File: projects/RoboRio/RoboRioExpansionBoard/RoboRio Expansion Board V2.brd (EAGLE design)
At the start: 56.6 x 77.5 mm, 133 parts, among them J1 RRINTERFACE-FEMALE, J10 SPI_MISO, J11 SPI_MOSI, J12 I2C_SCL, J13 I2C_SDA, J14 UART_TX, J15 UART_RX, J16 LCD, J17 ADC1, J18 ADC2, J19 ADC3, J2 MICROSD-HINGED, J20 ADC4, J21 ADC5, J22 ADC6, J23 ADC7, J25 PWM0, J26 PWM1, J27 PWM2, J28 PWM3, J29 PWM4, J3 51387-0578, J30 PWM5, J31 PWM6, J32 PWM7, J33 PWM8, J34 PWM9, J35 AI0, J36 AI1, J37 AI2, J38 AI3, J39 AO0, J4 GPIO0, J40 AO1, J5 GPIO1, J6 GPIO2, J7 GPIO3, J8 SPI_CS, J9 SPI_CLK, Q1 NPN-SOT416, Q2 NPN-SOT416, Q3 NPN-SOT416, SW1 450-1781-ND, U1 FTS31XS-U, U2 24LC256ST, U3 REG1117, U4 TPS2115APWR, U5 P8X32A-Q44_P, U6 TC54VN43, U7 ADC124S01, U8 ADC124S01, Y1 5MHz

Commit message: More silk
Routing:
- net +3V3: track 245.5 -> 244.4 mm
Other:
- board text added: "8"
- board text added: "9"
- board text added: "R11 R12 R13 R14 R15 R16"
- board text added: "RR PWM"

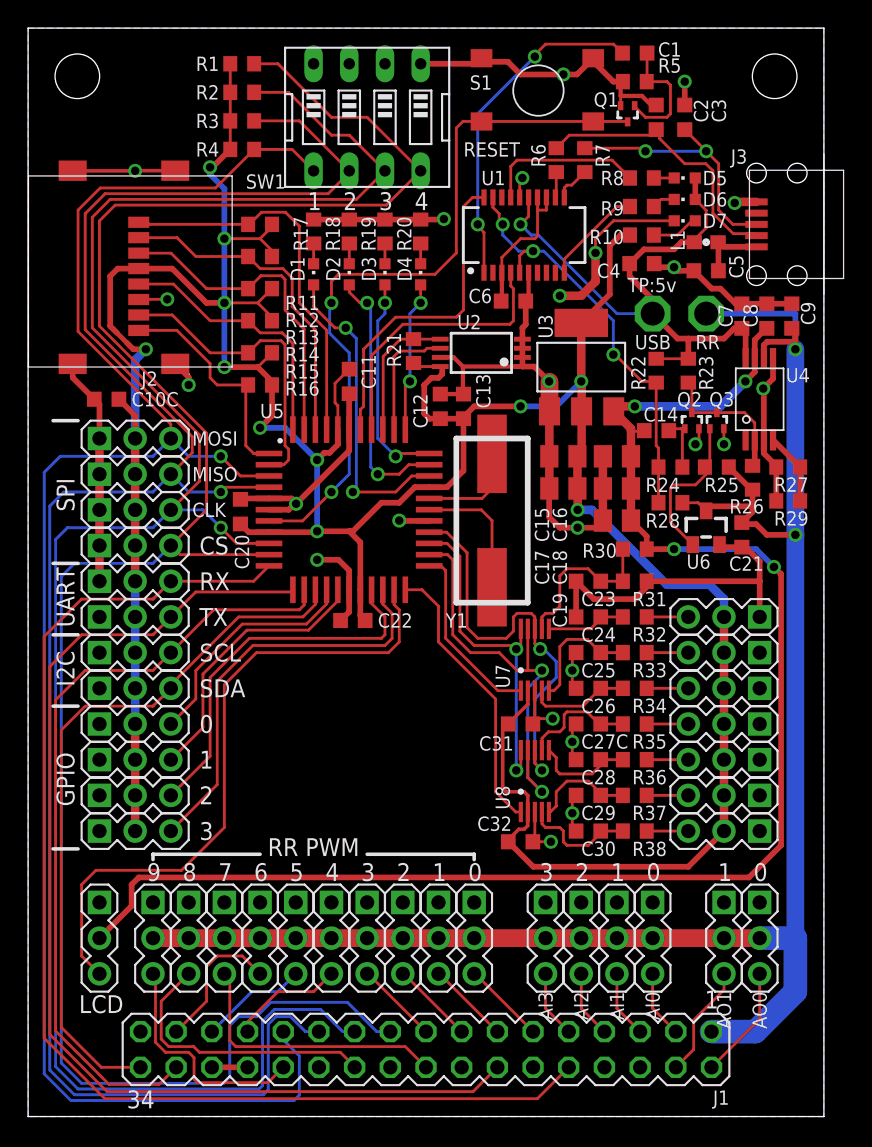
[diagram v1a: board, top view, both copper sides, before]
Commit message: copper under 3.3v regulator
D. Emge
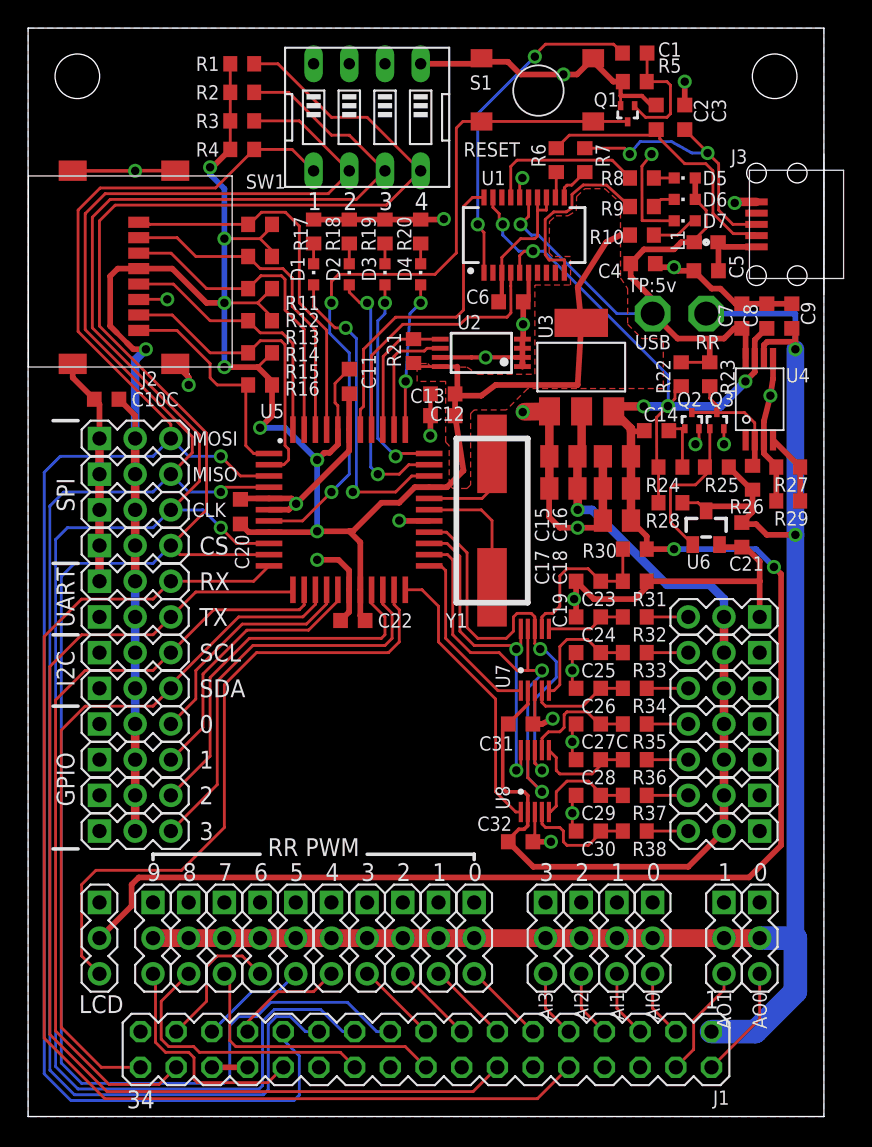
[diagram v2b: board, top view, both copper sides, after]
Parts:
- moved R22 1.80 mm to (46.5, 52.8)
- moved C13 1.61 mm to (29.5, 49.9), turned to 180 degrees
- moved R23 1.55 mm to (48.5, 52.8)
- moved C12 0.91 mm to (29.5, 51.4), turned to 0 degrees
- moved C6 0.18 mm to (34.4, 58.0)
- moved C4 0.08 mm to (43.8, 60.7)
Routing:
- net DGND: track 205.9 -> 198.4 mm, vias 24 -> 26
- net N$6: track 7.19 -> 13.1 mm
- net +3V3: track 244.4 -> 239.6 mm, vias 11 -> 9
- net PWREN_L: track 30.8 -> 33.2 mm
- net N$20: track 10.1 -> 11.7 mm
- net N$1: track 18.6 -> 19.4 mm
- net IO30_TX: track 19.9 -> 19.3 mm
- added copper zone on layer 1, net +3V3

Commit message: USB shield, other fun stuff
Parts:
- moved C22 1.27 mm to (23.1, 34.0)
- moved R22 0.51 mm to (46.5, 53.3)
- moved R23 0.51 mm to (48.5, 53.3)
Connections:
- net DGND: now also J3.P$1, J3.P$2, J3.P$3, J3.P$4
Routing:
- net DGND: track 198.4 -> 191.1 mm
- net +3V3: track 239.6 -> 242.6 mm, vias 9 -> 8
- net IO24: track 22.5 -> 20.2 mm
- net !RESET: track 52.5 -> 53.6 mm
- net IO25: track 18.5 -> 17.7 mm
- net IO17: track 29.5 -> 30.1 mm
- net IO16: track 26.9 -> 27.5 mm
- net IO18: track 46.5 -> 47.0 mm
- net PWREN_L: track 33.2 -> 33.8 mm
- net N$20: track 11.7 -> 12.2 mm
- net 5VUSB: track 42.4 -> 41.9 mm

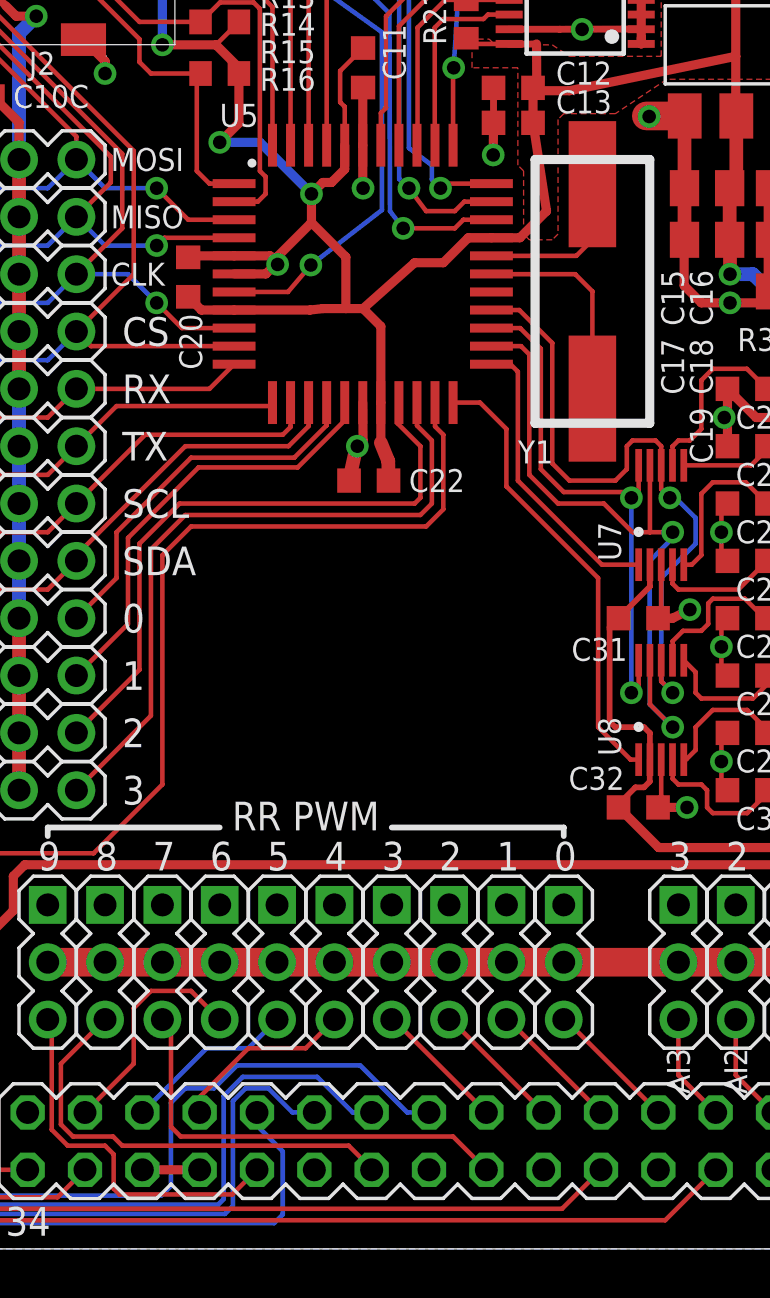
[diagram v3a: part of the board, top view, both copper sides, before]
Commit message: +3V3 pour
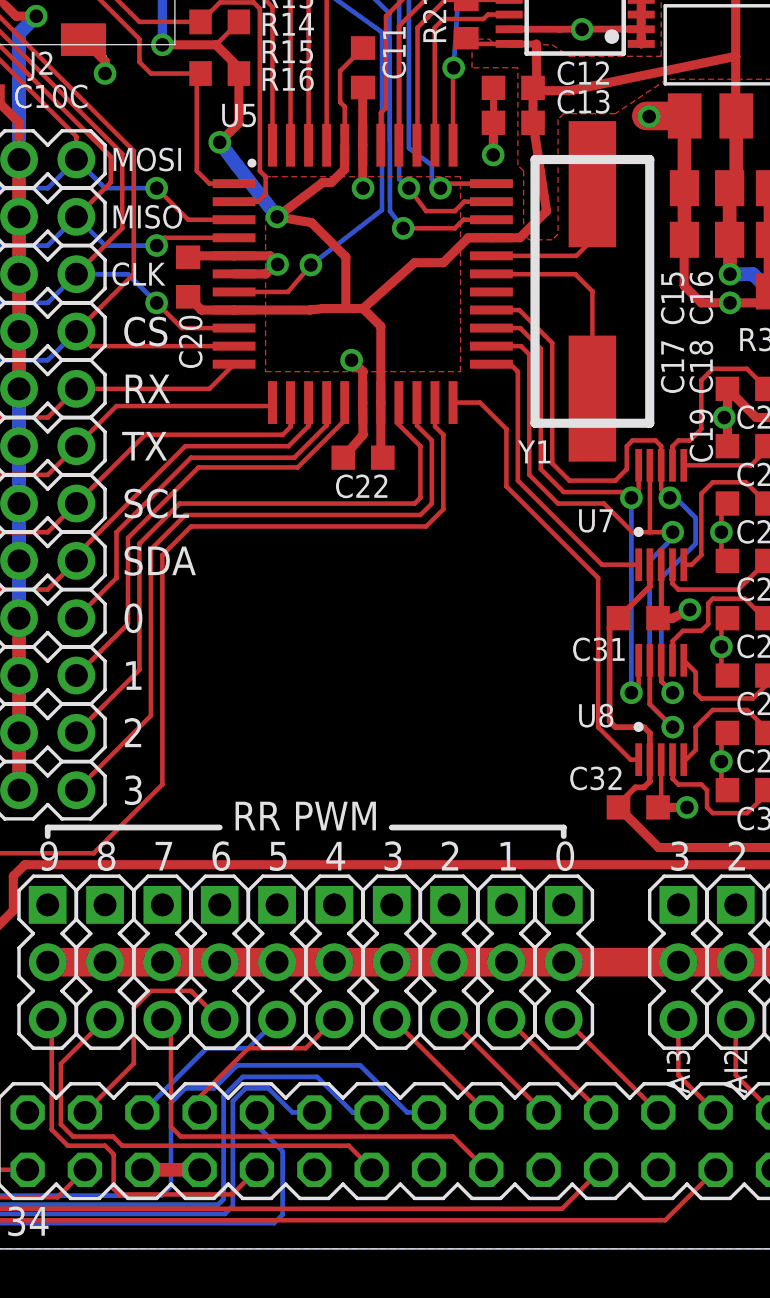
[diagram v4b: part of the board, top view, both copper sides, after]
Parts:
- moved C22 1.05 mm to (22.9, 35.1)
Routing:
- net DGND: track 191.1 -> 190.2 mm
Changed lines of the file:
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@@
 <attribute name="VALUE" x="28.7148" y="49.785" size="1.016" layer="27"/>
 </element>
-<element name="C22" library="resistor" package="C0603K" value="1uF" x="23.114" y="34.036" smashed="yes" rot="R180">
-<attribute name="NAME" x="24.892" y="33.528" size="1.016" layer="25" font="vector" ratio="14"/>
-<attribute name="VALUE" x="23.914" y="35.686" size="1.016" layer="27" rot="R180"/>
+<element name="C22" library="resistor" package="C0603K" value="1uF" x="22.86" y="35.052" smashed="yes" rot="R180">
+<attribute name="NAME" x="21.59" y="33.274" size="1.016" layer="25" font="vector" ratio="14"/>
+<attribute name="VALUE" x="23.66" y="36.702" size="1.016" layer="27" rot="R180"/>
 </element>
 <element name="C4" library="resistor" package="C0603K" value="4.7uF" x="43.7642" y="60.706" smashed="yes" rot="R180">
@@
 </element>
 <element name="U8" library="adc124s021cimm" package="ADC124S021VSSOP" value="ADC124S01" x="36.068" y="23.876" smashed="yes">
-<attribute name="NAME" x="34.29" y="21.844" size="1.016" layer="25" font="vector" ratio="14" rot="R90"/>
+<attribute name="NAME" x="34.036" y="24.13" size="1.016" layer="25" font="vector" ratio="14" rot="R180"/>
 <attribute name="VALUE" x="39.068" y="20.876" size="1.016" layer="27" rot="R90"/>
 </element>
 <element name="U7" library="adc124s021cimm" package="ADC124S021VSSOP" value="ADC124S01" x="36.068" y="32.512" smashed="yes">
-<attribute name="NAME" x="34.29" y="30.48" size="1.016" layer="25" font="vector" ratio="14" rot="R90"/>
+<attribute name="NAME" x="34.036" y="32.766" size="1.016" layer="25" font="vector" ratio="14" rot="R180"/>
 <attribute name="VALUE" x="39.068" y="29.512" size="1.016" layer="27" rot="R90"/>
 </element>
@@
 <wire x1="35.568" y1="22.852" x2="35.568" y2="21.676" width="0.254" layer="1"/>
 <wire x1="35.955" y1="17.78" x2="34.177" y2="19.558" width="0.4064" layer="1"/>
-<wire x1="23.6475" y1="37.4925" x2="23.6475" y2="35.7124" width="0.4064" layer="1"/>
-<wire x1="23.6475" y1="35.7124" x2="23.9776" y2="34.8996" width="0.6096" layer="1"/>
-<wire x1="23.9776" y1="34.8996" x2="23.989" y2="34.036" width="0.6096" layer="1"/>
+<wire x1="23.6475" y1="37.4925" x2="23.6475" y2="35.1395" width="0.4064" layer="1"/>
 <wire x1="28.5475" y1="44.7925" x2="29.8065" y2="44.7925" width="0.4064" layer="1"/>
 <wire x1="29.8065" y1="44.7925" x2="30.988" y2="45.974" width="0.4064" layer="1"/>
@@
 <wire x1="39.116" y1="44.688" x2="39.116" y2="43.18" width="0.6096" layer="1"/>
 <wire x1="49.53" y1="36.83" x2="49.53" y2="35.56" width="0.6096" layer="16"/>
-<via x="20.574" y="46.736" extent="1-16" drill="0.6" shape="square"/>
+<via x="19.05" y="45.72" extent="1-16" drill="0.6" shape="square"/>
 <wire x1="22.0475" y1="48.8925" x2="22.0475" y2="47.8285" width="0.4064" layer="1"/>
 <wire x1="22.0475" y1="47.8285" x2="21.463" y2="47.244" width="0.4064" layer="1"/>
 <wire x1="21.463" y1="47.244" x2="21.082" y2="47.244" width="0.4064" layer="1"/>
-<wire x1="21.082" y1="47.244" x2="20.574" y2="46.736" width="0.4064" layer="1"/>
+<wire x1="21.082" y1="47.244" x2="19.05" y2="45.72" width="0.4064" layer="1"/>
 <wire x1="17.1475" y1="41.5925" x2="20.5105" y2="41.5925" width="0.4064" layer="1"/>
 <wire x1="20.5105" y1="41.5925" x2="21.082" y2="41.656" width="0.4064" layer="1"/>
@@
 <wire x1="17.36" y1="49.872" x2="16.51" y2="49.022" width="0.4064" layer="1"/>
 <via x="16.51" y="49.022" extent="1-16" drill="0.6" shape="square"/>
-<wire x1="20.574" y1="46.736" x2="18.288" y2="49.022" width="0.4064" layer="16"/>
-<wire x1="18.288" y1="49.022" x2="16.51" y2="49.022" width="0.4064" layer="16"/>
+<wire x1="19.05" y1="45.72" x2="17.272" y2="48.006" width="0.6096" layer="16"/>
+<wire x1="17.272" y1="48.006" x2="16.51" y2="49.022" width="0.6096" layer="16"/>
 <wire x1="14.39" y1="68.834" x2="13.12" y2="67.564" width="0.4064" layer="1"/>
 <wire x1="13.12" y1="67.564" x2="12.954" y2="67.564" width="0.4064" layer="1"/>
@@
 <wire x1="21.082" y1="41.656" x2="22.098" y2="41.656" width="0.4064" layer="1"/>
 <wire x1="22.098" y1="41.656" x2="22.86" y2="41.656" width="0.4064" layer="1"/>
-<wire x1="20.574" y1="46.736" x2="20.574" y2="45.466" width="0.4064" layer="1"/>
+<wire x1="19.05" y1="45.72" x2="20.574" y2="45.466" width="0.4064" layer="1"/>
 <wire x1="20.574" y1="45.466" x2="22.098" y2="43.942" width="0.4064" layer="1"/>
 <wire x1="22.098" y1="43.942" x2="22.098" y2="41.656" width="0.4064" layer="1"/>
+<polygon width="0.254" layer="1">
+<vertex x="27.178" y="38.862"/>
+<vertex x="27.178" y="47.498"/>
+<vertex x="18.796" y="47.498"/>
+<vertex x="18.542" y="47.498"/>
+<vertex x="18.542" y="38.862"/>
+</polygon>
+<wire x1="23.6475" y1="35.1395" x2="23.735" y2="35.052" width="0.4064" layer="1"/>
 <wire x1="35.56" y1="21.668" x2="35.568" y2="21.676" width="0" layer="19" extent="1-1"/>
 <wire x1="39.37" y1="50.8" x2="39.3954" y2="50.1904" width="0" layer="19" extent="1-1"/>
@@
 <wire x1="22.86" y1="51.449" x2="22.8475" y2="51.4365" width="0.2032" layer="1"/>
 <wire x1="22.8475" y1="51.4365" x2="22.8475" y2="48.8925" width="0.4064" layer="1"/>
-<wire x1="13.081" y1="3.5052" x2="15.621" y2="3.5052" width="0.4064" layer="1"/>
+<wire x1="13.081" y1="3.5052" x2="15.621" y2="3.5052" width="0.6096" layer="1"/>
 <wire x1="5.08" y1="38.1" x2="5.08" y2="40.64" width="0.6096" layer="1"/>
 <wire x1="5.08" y1="43.18" x2="5.08" y2="40.64" width="0.6096" layer="1"/>
@@
 <via x="39.116" y="41.91" extent="1-16" drill="0.6" shape="square"/>
 <wire x1="44.03" y1="38.1" x2="52.07" y2="38.1" width="0.4064" layer="1"/>
-<wire x1="22.8475" y1="37.4925" x2="22.86" y2="35.814" width="0.4064" layer="1"/>
-<wire x1="22.86" y1="35.814" x2="22.747" y2="35.814" width="0.4064" layer="1"/>
-<wire x1="22.747" y1="35.814" x2="22.5935" y2="35.6605" width="0.4064" layer="1" curve="90"/>
-<wire x1="22.5935" y1="35.6605" x2="22.239" y2="34.036" width="0.6096" layer="1"/>
+<wire x1="22.8475" y1="37.4925" x2="22.86" y2="36.068" width="0.4064" layer="1"/>
+<wire x1="22.86" y1="36.068" x2="21.985" y2="35.052" width="0.4064" layer="1"/>
+<wire x1="21.985" y1="35.052" x2="21.8315" y2="34.8985" width="0.4064" layer="1" curve="90"/>
 <via x="19.0754" y="43.6118" extent="1-16" drill="0.6" shape="square"/>
 <wire x1="17.1475" y1="43.9925" x2="18.7455" y2="43.9925" width="0.4064" layer="1"/>
@@
 <via x="46.736" y="73.66" extent="1-16" drill="0.6" shape="square"/>
 <wire x1="46.736" y1="71.995" x2="46.736" y2="73.66" width="0.4064" layer="1"/>
-<via x="22.606" y="35.56" extent="1-16" drill="0.6" shape="square"/>
+<via x="22.352" y="39.37" extent="1-16" drill="0.6" shape="square"/>
 <wire x1="28.6398" y1="51.435" x2="28.6398" y2="49.8856" width="0.3048" layer="1"/>
 <wire x1="35.183" y1="53.381" x2="35.1634" y2="54.0414" width="0.3048" layer="1"/>
@@
 <contactref element="J3" pad="P$4"/>
 <via x="22.86" y="46.99" extent="1-16" drill="0.6" shape="square"/>
-<wire x1="19.0754" y1="43.6118" x2="19.0754" y2="43.9674" width="0.4064" layer="1"/>
-<wire x1="19.0754" y1="43.9674" x2="20.574" y2="45.466" width="0.4064" layer="1"/>
+<wire x1="22.8475" y1="37.4925" x2="22.8475" y2="38.8495" width="0.4064" layer="1"/>
+<wire x1="22.8475" y1="38.8495" x2="22.86" y2="38.862" width="0.4064" layer="1"/>
+<wire x1="22.86" y1="38.862" x2="22.352" y2="39.37" width="0.4064" layer="1"/>
+<wire x1="21.8315" y1="34.8985" x2="21.985" y2="35.052" width="0.4064" layer="1"/>
 <wire x1="35.2298" y1="56.388" x2="35.2412" y2="56.4248" width="0" layer="19" extent="1-1"/>
-<wire x1="22.5935" y1="35.6605" x2="22.606" y2="35.56" width="0" layer="19" extent="1-1"/>
 <wire x1="22.8475" y1="46.8759" x2="22.86" y2="46.99" width="0" layer="19" extent="1-1"/>
 <wire x1="28.5475" y1="42.3925" x2="28.6258" y2="48.4632" width="0" layer="19" extent="1-1"/>

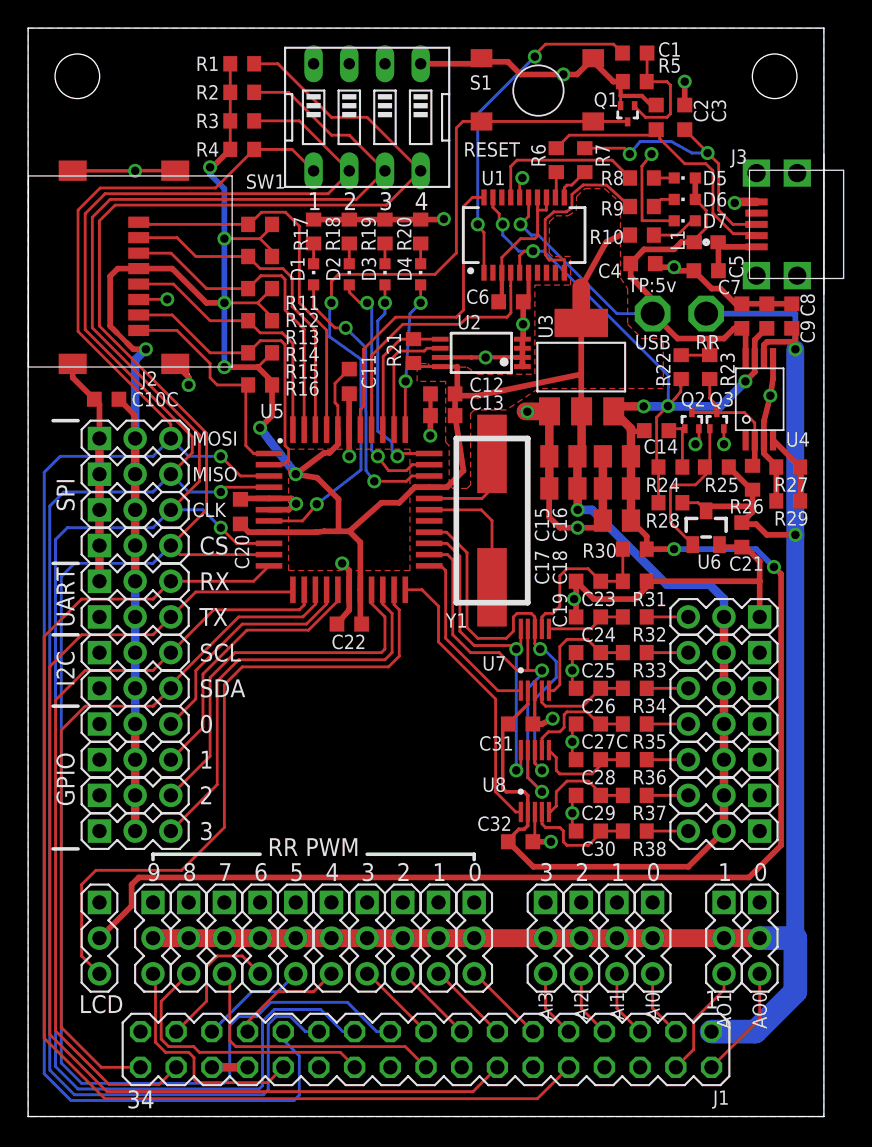
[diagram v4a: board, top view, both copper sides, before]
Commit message: Improve power routing
Please run DRCs in case I introduced routing errors.
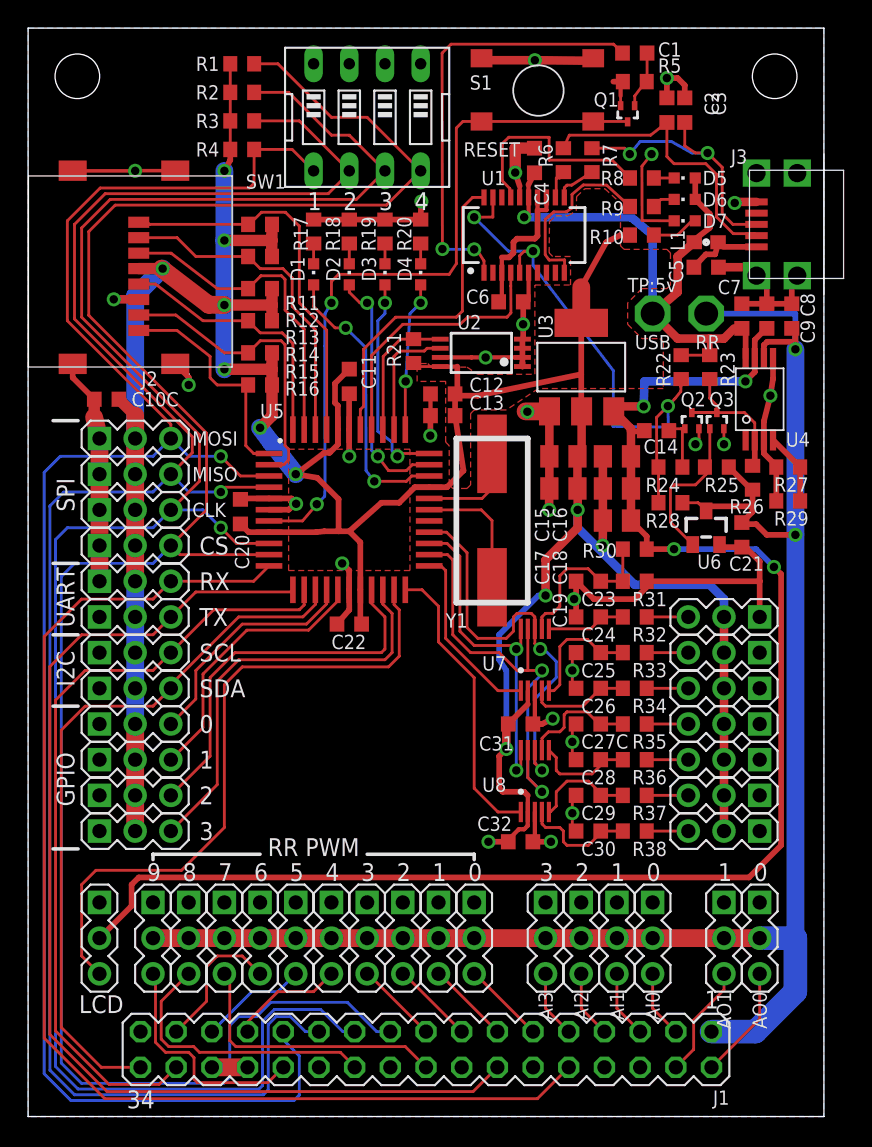
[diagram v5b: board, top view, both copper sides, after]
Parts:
- moved C4 10.7 mm to (36.0, 68.0), turned to 270 degrees
- moved C2 0.92 mm to (45.5, 71.6)
- moved R6 0.51 mm to (38.1, 68.1)
- moved C3 0.51 mm to (46.7, 71.6)
- moved R7 0.51 mm to (40.1, 68.1)
- moved C5 0.25 mm to (48.3, 60.5), turned to 180 degrees
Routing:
- net N$19: track 24.2 -> 31.5 mm
- net DGND: track 190.2 -> 183.5 mm
- net PWREN_L: track 33.8 -> 40.4 mm
- net N$26: track 8.90 -> 4.13 mm
- net N$7: track 11.4 -> 15.5 mm
- net IO6: track 123.2 -> 125.3 mm
- net !RESET: track 53.6 -> 51.7 mm
- net +3V3: track 242.9 -> 244.7 mm, vias 8 -> 11
- net 5VUSB: track 41.9 -> 43.6 mm
- net N$2: track 19.9 -> 21.2 mm
- net +5V: track 108.2 -> 109.2 mm
- net N$28: track 4.91 -> 5.68 mm
- net IO19: track 20.1 -> 20.9 mm
- net N$27: track 2.95 -> 3.62 mm
- net N$1: track 19.4 -> 20.1 mm
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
